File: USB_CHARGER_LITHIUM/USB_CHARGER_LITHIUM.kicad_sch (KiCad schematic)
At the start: 8 parts, among them J1 USB4135

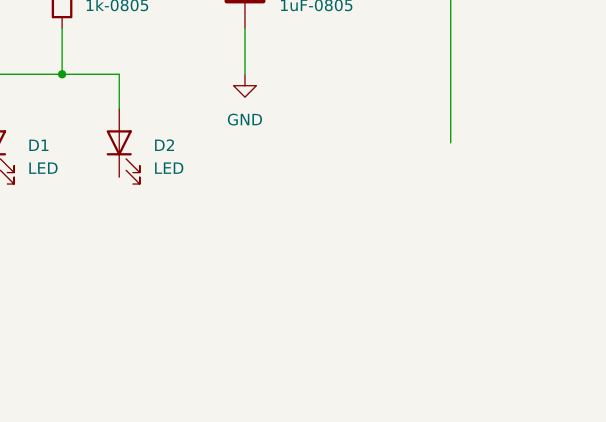
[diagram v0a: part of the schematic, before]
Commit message: Added battery chip regulator footprint/3d model
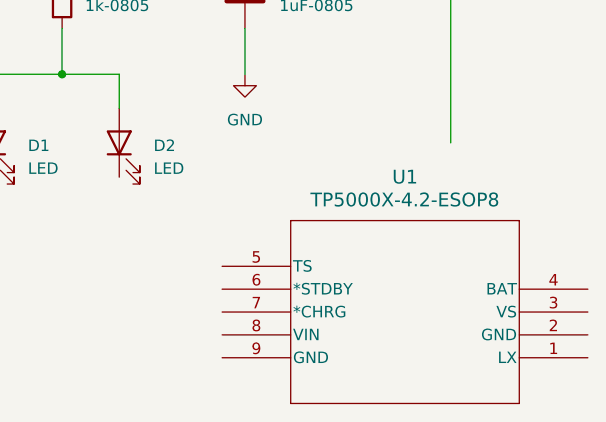
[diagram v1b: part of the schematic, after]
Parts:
- added U1: TP5000X-4.2-ESOP8, ESOP8_TPW, symbol ul_TP5000X-4-2-ESOP8:TP5000X-4.2-ESOP8
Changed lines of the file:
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@@
+	)
+	(symbol
+		(lib_id "ul_TP5000X-4-2-ESOP8:TP5000X-4.2-ESOP8")
+		(at 185.42 101.346 180)
+		(unit 1)
+		(exclude_from_sim no)
+		(in_bom yes)
+		(on_board yes)
+		(dnp no)
+		(fields_autoplaced yes)
+		(property "Reference" "U1"
+			(at 165.1 81.28 0)
+			(effects
+				(font
+					(size 1.524 1.524)
+				)
+			)
+		)
+		(property "Value" "TP5000X-4.2-ESOP8"
+			(at 165.1 83.82 0)
+			(effects
+				(font
+					(size 1.524 1.524)
+				)
+			)
+		)
+		(property "Footprint" "ESOP8_TPW"
+			(at 185.42 101.346 0)
+			(effects
+				(font
+					(size 1.27 1.27)
+					(italic yes)
+				)
+				(hide yes)
+			)
+		)
+		(property "Datasheet" "TP5000X-4.2-ESOP8"
+			(at 185.42 101.346 0)
+			(effects
+				(font
+					(size 1.27 1.27)
+					(italic yes)
+				)
+				(hide yes)
+			)
+		)
+		(property "Description" ""
+			(at 185.42 101.346 0)
+			(effects
+				(font
+					(size 1.27 1.27)
+				)
+				(hide yes)
+			)
+		)
+		(pin "5"
+		)
+		(pin "6"
+		)
+		(pin "7"
+		)
+		(pin "8"
+		)
+		(pin "1"
+		)
+		(pin "9"
+		)
+		(pin "4"
+		)
+		(pin "3"
+		)
+		(pin "2"
+		)
+		(instances
+			(project ""
+				(path "/740b141e-76db-4770-b8b7-f30b8f055222"
+					(reference "U1")
+					(unit 1)
+				)
+			)
+		)
 	)
 	(symbol

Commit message: Working on wiring IC
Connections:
- net GND: now also U1.5 (TS)
- net at C1.1, C2.1, J1.A9 (VBUS)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: now also U1.8 (VIN)
- net at D2.1 (K): now also U1.7 (*CHRG)
- net at D1.1 (K): now also U1.6 (*STDBY)
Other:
- moved on the sheet: C2
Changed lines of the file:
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@@
 	(paper "A4")
-	(junction
-		(at 147.32 49.53)
-		(diameter 0)
-		(color 0 0 0 0)
-	)
 	(junction
 		(at 105.41 49.53)
@@
 		(color 0 0 0 0)
 	)
-	(wire
-		(pts
-			(xy 147.32 49.53) (xy 170.18 49.53)
+	(junction
+		(at 144.018 49.53)
+		(diameter 0)
+		(color 0 0 0 0)
+	)
+	(wire
+		(pts
+			(xy 119.38 93.726) (xy 132.334 93.726)
+		)
+		(stroke
+			(width 0)
+			(type default)
+		)
+	)
+	(wire
+		(pts
+			(xy 133.35 96.266) (xy 144.78 96.266)
 		)
 		(stroke
@@
 	(wire
 		(pts
-			(xy 147.32 64.77) (xy 147.32 69.85)
+			(xy 144.018 64.77) (xy 144.018 69.85)
+		)
+		(stroke
+			(width 0)
+			(type default)
+		)
+	)
+	(wire
+		(pts
+			(xy 140.208 91.186) (xy 140.208 112.268)
 		)
 		(stroke
@@
 	(wire
 		(pts
-			(xy 127 49.53) (xy 147.32 49.53)
+			(xy 127 49.53) (xy 144.018 49.53)
+		)
+		(stroke
+			(width 0)
+			(type default)
+		)
+	)
+	(wire
+		(pts
+			(xy 144.78 91.186) (xy 140.208 91.186)
 		)
 		(stroke
@@
 	(wire
 		(pts
+			(xy 134.366 92.71) (xy 134.366 93.726)
+		)
+		(stroke
+			(width 0)
+			(type default)
+		)
+	)
+	(wire
+		(pts
+			(xy 132.334 93.726) (xy 132.334 92.71)
+		)
+		(stroke
+			(width 0)
+			(type default)
+		)
+	)
+	(wire
+		(pts
 			(xy 77.47 62.23) (xy 77.47 69.85)
 		)
@@
 	(wire
 		(pts
+			(xy 144.018 49.53) (xy 163.83 49.53)
+		)
+		(stroke
+			(width 0)
+			(type default)
+		)
+	)
+	(wire
+		(pts
 			(xy 64.77 64.77) (xy 64.77 69.85)
 		)
@@
 	(wire
 		(pts
-			(xy 170.18 49.53) (xy 170.18 77.47)
-		)
-		(stroke
-			(width 0)
-			(type default)
-		)
-	)
-	(wire
-		(pts
 			(xy 64.77 77.47) (xy 64.77 81.28)
 		)
@@
 	(wire
 		(pts
+			(xy 134.366 93.726) (xy 144.78 93.726)
+		)
+		(stroke
+			(width 0)
+			(type default)
+		)
+	)
+	(wire
+		(pts
+			(xy 163.83 49.53) (xy 163.83 78.486)
+		)
+		(stroke
+			(width 0)
+			(type default)
+		)
+	)
+	(wire
+		(pts
+			(xy 133.35 81.28) (xy 133.35 96.266)
+		)
+		(stroke
+			(width 0)
+			(type default)
+		)
+	)
+	(wire
+		(pts
 			(xy 133.35 69.85) (xy 133.35 73.66)
 		)
@@
 	(wire
 		(pts
-			(xy 147.32 49.53) (xy 147.32 57.15)
+			(xy 144.018 49.53) (xy 144.018 57.15)
 		)
 		(stroke
@@
 		(pts
 			(xy 127 69.85) (xy 133.35 69.85)
+		)
+		(stroke
+			(width 0)
+			(type default)
+		)
+	)
+	(wire
+		(pts
+			(xy 132.334 92.71) (xy 134.366 92.71)
+		)
+		(stroke
+			(width 0)
+			(type default)
+		)
+	)
+	(wire
+		(pts
+			(xy 119.38 81.28) (xy 119.38 93.726)
 		)
 		(stroke
@@
 	(symbol
 		(lib_id "Device:C")
-		(at 147.32 60.96 0)
+		(at 144.018 60.96 0)
 		(unit 1)
 		(exclude_from_sim no)
@@
 		(fields_autoplaced yes)
 		(property "Reference" "C2"
-			(at 151.13 59.6899 0)
+			(at 147.828 59.6899 0)
 			(effects
 				(font
@@
 		)
 		(property "Value" "1uF-0805"
-			(at 151.13 62.2299 0)
+			(at 147.828 62.2299 0)
 			(effects
 				(font
@@
 		)
 		(property "Footprint" ""
-			(at 148.2852 64.77 0)
+			(at 144.9832 64.77 0)
 			(effects
 				(font
@@
 		)
 		(property "Datasheet" "~"
-			(at 147.32 60.96 0)
+			(at 144.018 60.96 0)
 			(effects
 				(font
@@
 		)
 		(property "Description" "Unpolarized capacitor"
-			(at 147.32 60.96 0)
+			(at 144.018 60.96 0)
 			(effects
 				(font
@@
 	(symbol
 		(lib_id "power:GND")
-		(at 147.32 69.85 0)
+		(at 144.018 69.85 0)
 		(unit 1)
 		(exclude_from_sim no)
@@
 		(fields_autoplaced yes)
 		(property "Reference" "#PWR06"
-			(at 147.32 76.2 0)
+			(at 144.018 76.2 0)
 			(effects
 				(font
@@
 		)
 		(property "Value" "GND"
-			(at 147.32 74.93 0)
+			(at 144.018 74.93 0)
 			(effects
 				(font
@@
 		)
 		(property "Footprint" ""
-			(at 147.32 69.85 0)
+			(at 144.018 69.85 0)
 			(effects
 				(font
@@
 		)
 		(property "Datasheet" ""
-			(at 147.32 69.85 0)
+			(at 144.018 69.85 0)
 			(effects
 				(font
@@
 		)
 		(property "Description" "Power symbol creates a global label with name \"GND\" , ground"
-			(at 147.32 69.85 0)
+			(at 144.018 69.85 0)
 			(effects
 				(font
@@
 		(on_board yes)
 		(dnp no)
-		(fields_autoplaced yes)
 		(property "Reference" "U1"
-			(at 165.1 81.28 0)
+			(at 168.402 80.518 0)
 			(effects
 				(font
@@
 		)
 		(property "Value" "TP5000X-4.2-ESOP8"
-			(at 165.1 83.82 0)
+			(at 179.324 83.312 0)
 			(effects
 				(font
@@
 		)
 		(pin "1"
-		)
-		(pin "9"
 		)
 		(pin "4"
@@
 					(unit 1)
 				)
+			)
+		)
+	)
+	(symbol
+		(lib_id "power:GND")
+		(at 140.208 112.268 0)
+		(unit 1)
+		(exclude_from_sim no)
+		(in_bom yes)
+		(on_board yes)
+		(dnp no)
+		(fields_autoplaced yes)
+		(property "Reference" "#PWR07"
+			(at 140.208 118.618 0)
+			(effects
+				(font
+					(size 1.27 1.27)
+				)
+				(hide yes)
+			)
+		)
+		(property "Value" "GND"
+			(at 140.208 116.84 0)
+			(effects
+				(font
+					(size 1.27 1.27)
+				)
+			)
+		)
+		(property "Footprint" ""
+			(at 140.208 112.268 0)
+			(effects
+				(font
+					(size 1.27 1.27)
+				)
+				(hide yes)
+			)
+		)
+		(property "Datasheet" ""
+			(at 140.208 112.268 0)
+			(effects
+				(font
+					(size 1.27 1.27)
+				)
+				(hide yes)
+			)
+		)
+		(property "Description" "Power symbol creates a global label with name \"GND\" , ground"
+			(at 140.208 112.268 0)
+			(effects
+				(font
+					(size 1.27 1.27)
+				)
+				(hide yes)
+			)
+		)
+		(pin "1"
+		)
+		(instances
+			(project ""
+				(path "/740b141e-76db-4770-b8b7-f30b8f055222"
+					(reference "#PWR07")
+					(unit 1)
+				)

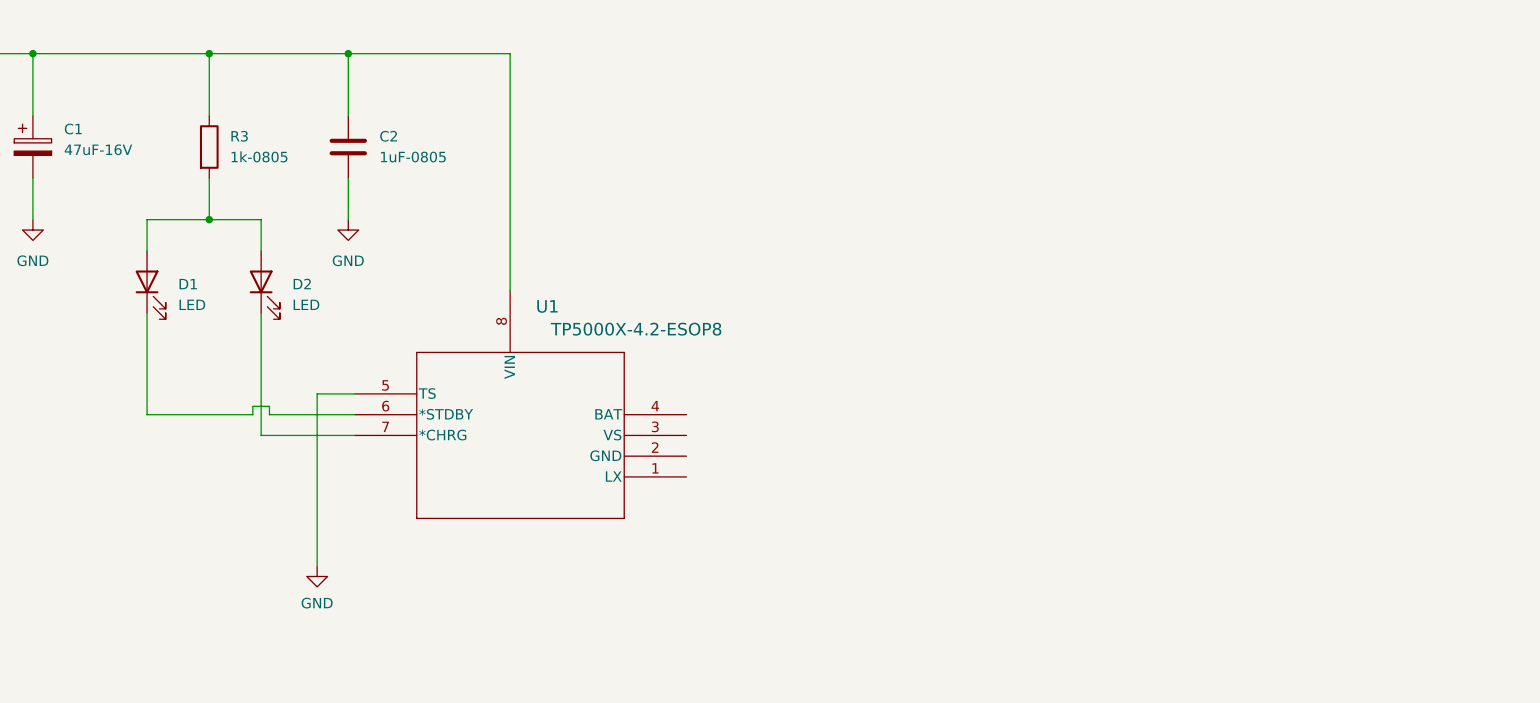
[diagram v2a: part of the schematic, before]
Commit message: Need to include battery management ic
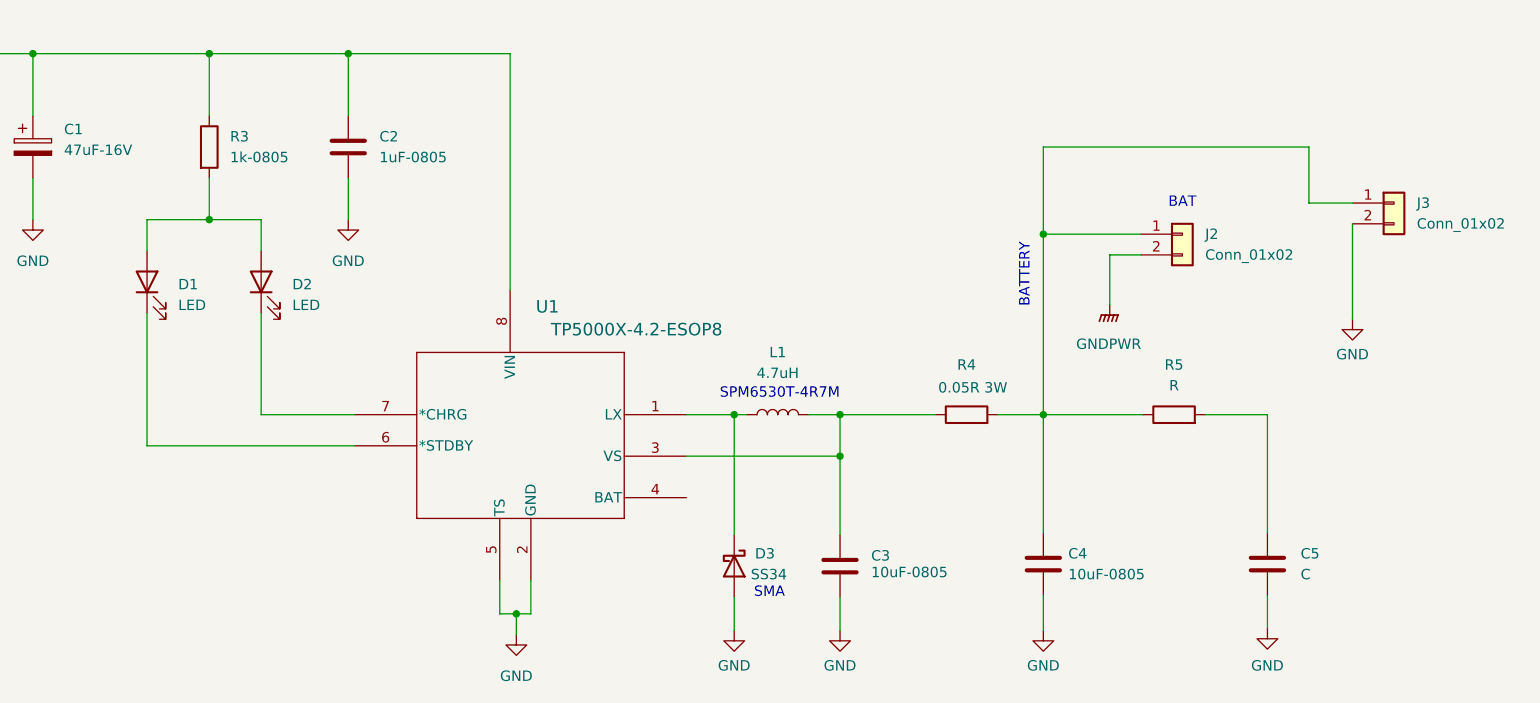
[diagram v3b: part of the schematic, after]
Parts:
- added C3, C4: 10uF-0805, symbol Device:C
- added C5: C, symbol Device:C
- added D3: SS34, Diode_SMD:D_SMA, symbol Diode:SS34
- added J2, J3: Conn_01x02, symbol Connector_Generic:Conn_01x02
- added L1: 4.7uH, symbol Device:L
- added R4: 0.05R 3W, symbol Device:R
- added R5: R, symbol Device:R
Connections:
- net GND: now also U1.2 (GND), C3.2, C4.2, C5.2, D3.2 (A), J3.2 (Pin_2)
- net at U1.1 (LX): now also D3.1 (K), L1.1
- net at U1.3 (VS): now also C3.1, L1.2, R4.1
- new net: C4.1, J2.1 (Pin_1), J3.1 (Pin_1), R4.2, R5.1
- new net: C5.1, R5.2
- new net GNDPWR: J2.2 (Pin_2)
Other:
- note added: "BAT"
- note added: "BATTERY"
- note added: "SMA"
- note added: "SPM6530T-4R7M"
- moved on the sheet: U1

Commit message: Finished Schematic
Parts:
- added U2: XB7608A, symbol XB7608A:XB7608A
- C5: value C -> 100nF-0805
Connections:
- net GND: now also U2.4 (VM), U2.5 (VM)
- net GNDPWR: now also U2.2 (GND), U2.3 (GND)
- net at C4.1, J2.1 (Pin_1), J3.1 (Pin_1)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: now also U1.4 (BAT)
- net at C5.1, R5.2: now also U2.1 (VDD)
- net at D2.1 (K): no longer U1.7 (*CHRG)
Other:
- note added: "USB C Switching Lithium Battery Charger ( 2 AMPS )"
- company: (none) -> VICTOR ROSALES
- title: (none) -> USB C Lithium Battery Charger (2AMP)
- moved on the sheet: C1, C2, C3, C4, C5, D1, D2, D3, J1, J2, J3, L1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

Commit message: Added libraries and assigned footprints
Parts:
- added H1, H2, H3: MountingHole, MountingHole:MountingHole_3.2mm_M3_DIN965_Pad, symbol Mechanical:MountingHole
- C1: footprint (none) -> Capacitor_THT:CP_Radial_D10.0mm_P5.00mm
- C2, C3, C4, C5: footprint (none) -> Capacitor_SMD:C_0805_2012Metric
- D1, D2: footprint (none) -> LED_SMD:LED_0805_2012Metric
- J1: footprint (none) -> Connector_USB:USB_C_Receptacle_GCT_USB4135-GF-A_6P_TopMnt_Horizontal
- J2: footprint (none) -> Connector_JST:JST_XH_B2B-XH-A_1x02_P2.50mm_Vertical
- J3: footprint (none) -> Connector_JST:JST_PH_B2B-PH-K_1x02_P2.00mm_Vertical
- L1: footprint (none) -> lcsc_footprints:C76857_IND-SMD_L7_1-W6_5
- R1, R2, R3: footprint (none) -> Resistor_SMD:R_0805_2012Metric
- R4: footprint (none) -> Resistor_SMD:R_2512_6332Metric
- R5: value R -> 1k-0805; footprint (none) -> Resistor_SMD:R_0805_2012Metric
- U1: footprint ESOP8_TPW -> lcsc_footprints:C5447152_ESOP-8_L4_9-W3_9-P1_27-LS6_0-BL-EP
- U2: footprint (none) -> lcsc_footprints:C669688_CPC-5_L2_6-W2_6-LS4_2_XB7608A
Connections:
- net at D2.1 (K): now also U1.7 (*CHRG)
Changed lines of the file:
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@@
 	(wire
 		(pts
-			(xy 106.68 92.71) (xy 118.11 92.71)
+			(xy 106.68 92.71) (xy 119.38 92.71)
 		)
 		(stroke
@@
 			)
 		)
-		(property "Footprint" ""
+		(property "Footprint" "Connector_USB:USB_C_Receptacle_GCT_USB4135-GF-A_6P_TopMnt_Horizontal"
 			(at 34.544 53.594 0)
 			(effects
@@
 			)
 		)
-		(property "Footprint" ""
+		(property "Footprint" "Connector_JST:JST_PH_B2B-PH-K_1x02_P2.00mm_Vertical"
 			(at 244.094 67.056 0)
 			(effects
@@
 			)
 		)
-		(property "Footprint" ""
+		(property "Footprint" "Connector_JST:JST_XH_B2B-XH-A_1x02_P2.50mm_Vertical"
 			(at 218.186 70.866 0)
 			(effects
@@
 			)
 		)
-		(property "Footprint" ""
+		(property "Footprint" "Resistor_SMD:R_0805_2012Metric"
 			(at 98.552 59.944 90)
 			(effects
@@
 			)
 		)
-		(property "Footprint" ""
+		(property "Footprint" "Capacitor_SMD:C_0805_2012Metric"
 			(at 118.3132 63.754 0)
 			(effects
@@
 			)
 		)
-		(property "Value" "R"
+		(property "Value" "1k-0805"
 			(at 218.44 88.9 90)
 			(effects
@@
 			)
 		)
-		(property "Footprint" ""
+		(property "Footprint" "Resistor_SMD:R_0805_2012Metric"
 			(at 218.44 94.234 90)
 			(effects
@@
 			)
 		)
-		(property "Footprint" ""
+		(property "Footprint" "lcsc_footprints:C76857_IND-SMD_L7_1-W6_5"
 			(at 169.926 92.456 0)
 			(effects
@@
 			)
 		)
-		(property "Footprint" ""
+		(property "Footprint" "LED_SMD:LED_0805_2012Metric"
 			(at 106.68 76.454 0)
 			(effects
@@
 			)
 		)
-		(property "Footprint" ""
+		(property "Footprint" "Resistor_SMD:R_0805_2012Metric"
 			(at 51.816 72.644 90)
 			(effects
@@
 			)
 		)
-		(property "Footprint" ""
+		(property "Footprint" "Capacitor_SMD:C_0805_2012Metric"
 			(at 178.5112 114.808 0)
 			(effects
@@
 			)
 		)
-		(property "Footprint" ""
+		(property "Footprint" "LED_SMD:LED_0805_2012Metric"
 			(at 92.71 76.454 0)
 			(effects
@@
 			)
 		)
-		(property "Footprint" ""
+		(property "Footprint" "Resistor_SMD:R_0805_2012Metric"
 			(at 64.516 72.644 90)
 			(effects
@@
 	)
 	(symbol
+		(lib_id "Mechanical:MountingHole")
+		(at 58.42 153.67 0)
+		(unit 1)
+		(exclude_from_sim no)
+		(in_bom no)
+		(on_board yes)
+		(dnp no)
+		(fields_autoplaced yes)
+		(property "Reference" "H2"
+			(at 60.96 152.3999 0)
+			(effects
+				(font
+					(size 1.27 1.27)
+				)
+				(justify left)
+			)
+		)
+		(property "Value" "MountingHole"
+			(at 60.96 154.9399 0)
+			(effects
+				(font
+					(size 1.27 1.27)
+				)
+				(justify left)
+			)
+		)
+		(property "Footprint" "MountingHole:MountingHole_3.2mm_M3_DIN965_Pad"
+			(at 58.42 153.67 0)
+			(effects
+				(font
+					(size 1.27 1.27)
+				)
+				(hide yes)
+			)
+		)
+		(property "Datasheet" "~"
+			(at 58.42 153.67 0)
+			(effects
+				(font
+					(size 1.27 1.27)
+				)
+				(hide yes)
+			)
+		)
+		(property "Description" "Mounting Hole without connection"
+			(at 58.42 153.67 0)
+			(effects
+				(font
+					(size 1.27 1.27)
+				)
+				(hide yes)
+			)
+		)
+		(instances
+			(project "USB_CHARGER_LITHIUM"
+				(path "/740b141e-76db-4770-b8b7-f30b8f055222"
+					(reference "H2")
+					(unit 1)
+				)
+			)
+		)
+	)
+	(symbol
 		(lib_id "XB7608A:XB7608A")
 		(at 256.54 95.25 0)
@@
 			)
 		)
-		(property "Footprint" ""
+		(property "Footprint" "lcsc_footprints:C669688_CPC-5_L2_6-W2_6-LS4_2_XB7608A"
 			(at 256.54 95.25 0)
 			(effects
@@
 			)
 		)
-		(property "Footprint" ""
+		(property "Footprint" "Capacitor_THT:CP_Radial_D10.0mm_P5.00mm"
 			(at 80.9752 63.5 0)
 			(effects
@@
 	)
 	(symbol
+		(lib_id "Mechanical:MountingHole")
+		(at 88.9 153.67 0)
+		(unit 1)
+		(exclude_from_sim no)
+		(in_bom no)
+		(on_board yes)
+		(dnp no)
+		(fields_autoplaced yes)
+		(property "Reference" "H3"
+			(at 91.44 152.3999 0)
+			(effects
+				(font
+					(size 1.27 1.27)
+				)
+				(justify left)
+			)
+		)
+		(property "Value" "MountingHole"
+			(at 91.44 154.9399 0)
+			(effects
+				(font
+					(size 1.27 1.27)
+				)
+				(justify left)
+			)
+		)
+		(property "Footprint" "MountingHole:MountingHole_3.2mm_M3_DIN965_Pad"
+			(at 88.9 153.67 0)
+			(effects
+				(font
+					(size 1.27 1.27)
+				)
+				(hide yes)
+			)
+		)
+		(property "Datasheet" "~"
+			(at 88.9 153.67 0)
+			(effects
+				(font
+					(size 1.27 1.27)
+				)
+				(hide yes)
+			)
+		)
+		(property "Description" "Mounting Hole without connection"
+			(at 88.9 153.67 0)
+			(effects
+				(font
+					(size 1.27 1.27)
+				)
+				(hide yes)
+			)
+		)
+		(instances
+			(project "USB_CHARGER_LITHIUM"
+				(path "/740b141e-76db-4770-b8b7-f30b8f055222"
+					(reference "H3")
+					(unit 1)
+				)
+			)
+		)
+	)
+	(symbol
 		(lib_id "power:GNDPWR")
 		(at 256.54 113.03 0)
@@
 			)
 		)
-		(property "Footprint" ""
+		(property "Footprint" "Capacitor_SMD:C_0805_2012Metric"
 			(at 202.6412 115.316 0)
 			(effects
@@
 	)
 	(symbol
+		(lib_id "Mechanical:MountingHole")
+		(at 30.48 153.67 0)
+		(unit 1)
+		(exclude_from_sim no)
+		(in_bom no)
+		(on_board yes)
+		(dnp no)
+		(fields_autoplaced yes)
+		(property "Reference" "H1"
+			(at 33.02 152.3999 0)
+			(effects
+				(font
+					(size 1.27 1.27)
+				)
+				(justify left)
+			)
+		)
+		(property "Value" "MountingHole"
+			(at 33.02 154.9399 0)
+			(effects
+				(font
+					(size 1.27 1.27)
+				)
+				(justify left)
+			)
+		)
+		(property "Footprint" "MountingHole:MountingHole_3.2mm_M3_DIN965_Pad"
+			(at 30.48 153.67 0)
+			(effects
+				(font
+					(size 1.27 1.27)
+				)
+				(hide yes)
+			)
+		)
+		(property "Datasheet" "~"
+			(at 30.48 153.67 0)
+			(effects
+				(font
+					(size 1.27 1.27)
+				)
+				(hide yes)
+			)
+		)
+		(property "Description" "Mounting Hole without connection"
+			(at 30.48 153.67 0)
+			(effects
+				(font
+					(size 1.27 1.27)
+				)
+				(hide yes)
+			)
+		)
+		(instances
+			(project ""
+				(path "/740b141e-76db-4770-b8b7-f30b8f055222"
+					(reference "H1")
+					(unit 1)
+				)
+			)
+		)
+	)
+	(symbol
 		(lib_id "Device:R")
 		(at 193.04 92.456 90)
@@
 			)
 		)
-		(property "Footprint" ""
+		(property "Footprint" "Resistor_SMD:R_2512_6332Metric"
 			(at 193.04 94.234 90)
 			(effects
@@
 			)
 		)
-		(property "Footprint" "ESOP8_TPW"
+		(property "Footprint" "lcsc_footprints:C5447152_ESOP-8_L4_9-W3_9-P1_27-LS6_0-BL-EP"
 			(at 158.75 100.33 0)
 			(effects
@@
 			)
 		)
-		(property "Footprint" ""
+		(property "Footprint" "Capacitor_SMD:C_0805_2012Metric"
 			(at 230.8352 114.554 0)
 			(effects

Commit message: Placed components in pcb
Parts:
- removed H3: MountingHole, MountingHole:MountingHole_3.2mm_M3_DIN965_Pad, symbol Mechanical:MountingHole
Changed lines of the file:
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@@
-	)
-	(symbol
-		(lib_id "Mechanical:MountingHole")
-		(at 88.9 153.67 0)
-		(unit 1)
-		(exclude_from_sim no)
-		(in_bom no)
-		(on_board yes)
-		(dnp no)
-		(fields_autoplaced yes)
-		(property "Reference" "H3"
-			(at 91.44 152.3999 0)
-			(effects
-				(font
-					(size 1.27 1.27)
-				)
-				(justify left)
-			)
-		)
-		(property "Value" "MountingHole"
-			(at 91.44 154.9399 0)
-			(effects
-				(font
-					(size 1.27 1.27)
-				)
-				(justify left)
-			)
-		)
-		(property "Footprint" "MountingHole:MountingHole_3.2mm_M3_DIN965_Pad"
-			(at 88.9 153.67 0)
-			(effects
-				(font
-					(size 1.27 1.27)
-				)
-				(hide yes)
-			)
-		)
-		(property "Datasheet" "~"
-			(at 88.9 153.67 0)
-			(effects
-				(font
-					(size 1.27 1.27)
-				)
-				(hide yes)
-			)
-		)
-		(property "Description" "Mounting Hole without connection"
-			(at 88.9 153.67 0)
-			(effects
-				(font
-					(size 1.27 1.27)
-				)
-				(hide yes)
-			)
-		)
-		(instances
-			(project "USB_CHARGER_LITHIUM"
-				(path "/740b141e-76db-4770-b8b7-f30b8f055222"
-					(reference "H3")
-					(unit 1)
-				)
-			)
-		)
 	)
 	(symbol
